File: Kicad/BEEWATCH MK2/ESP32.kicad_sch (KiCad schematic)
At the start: 38 parts, among them Q1 DMG6968U, SW1 TK-074-4, SW2 TK-074-4, U1 ESP32-S3, Y1 40MHz

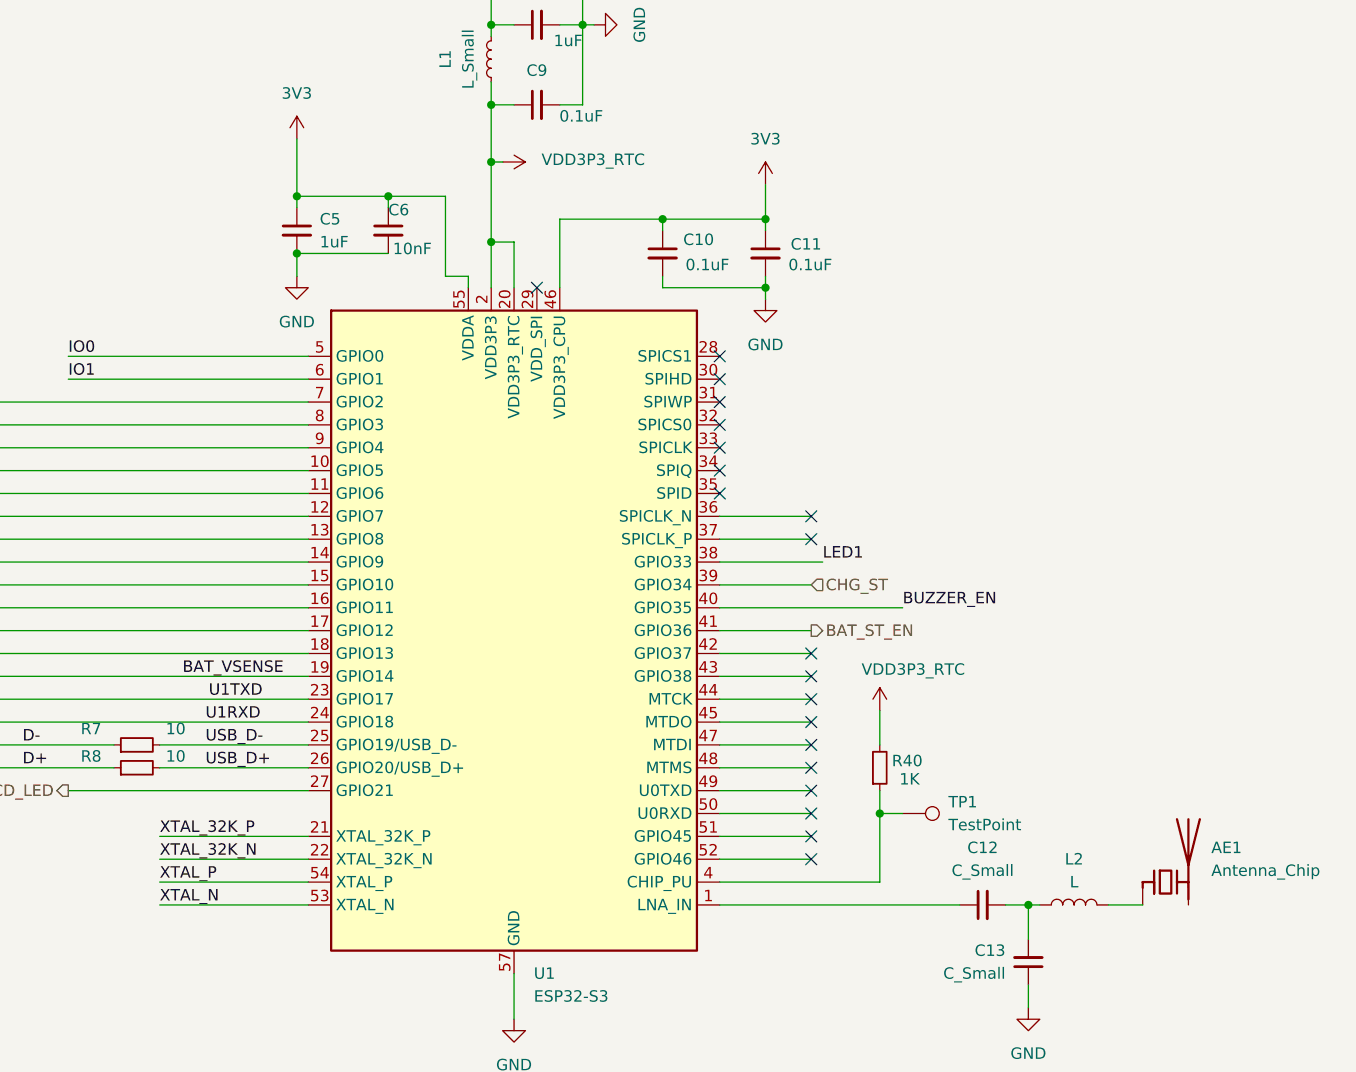
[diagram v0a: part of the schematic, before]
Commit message: Schematic changes
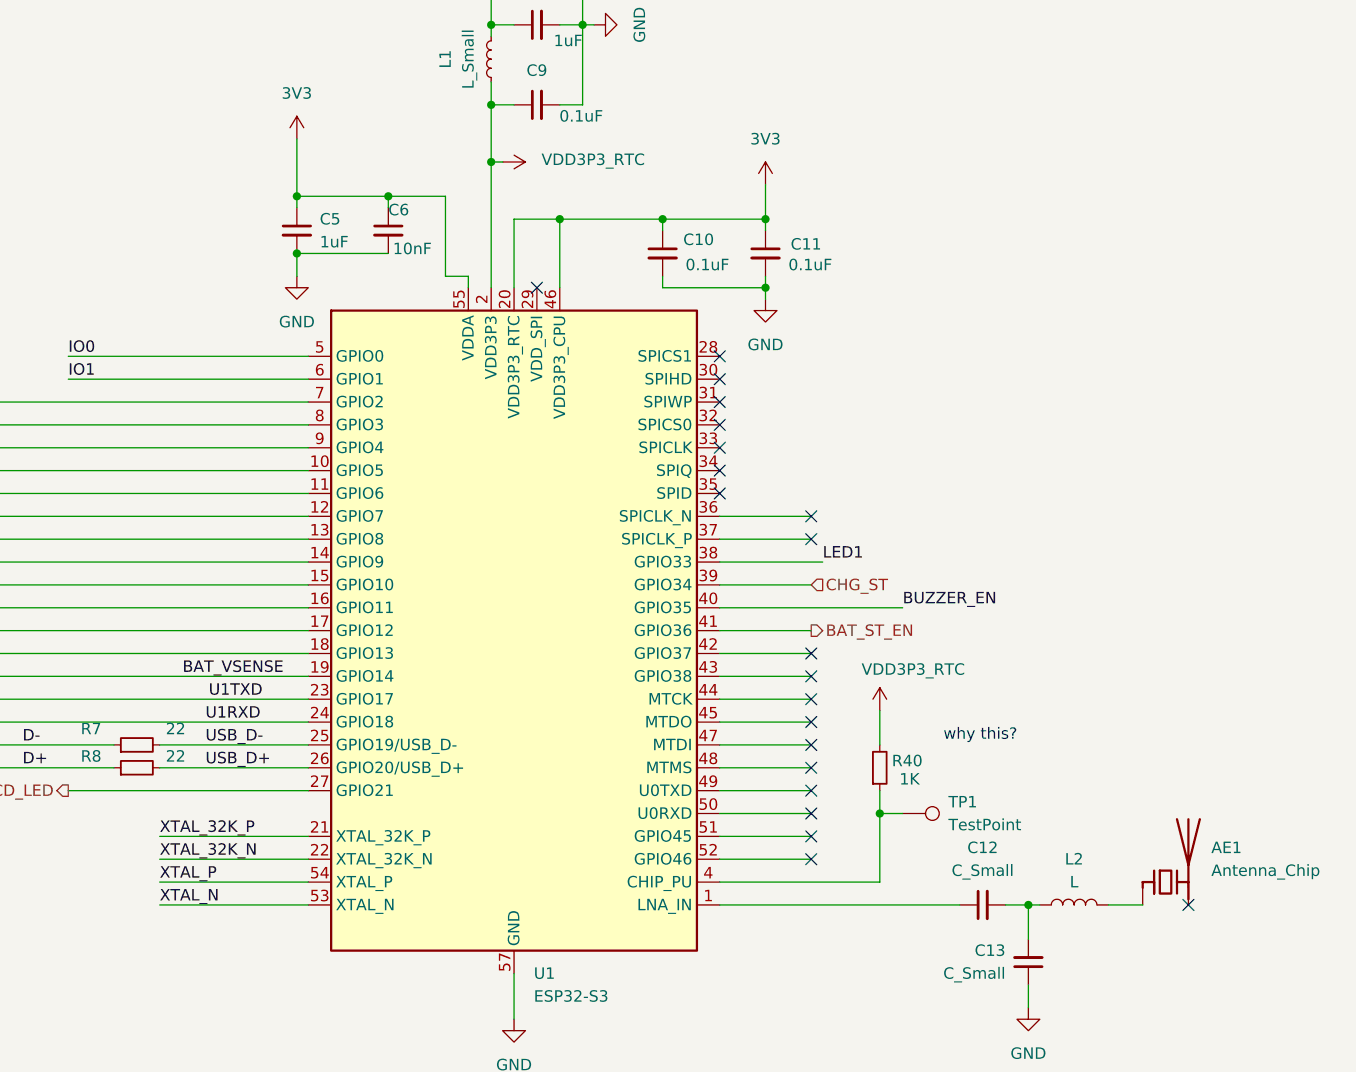
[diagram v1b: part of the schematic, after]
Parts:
- AE1: footprint (none) -> Project:ANT
- C10, C11, C12, C13, C5, C6, C7, C8, C9: footprint Capacitor_SMD:C_0603_1608Metric -> Capacitor_SMD:C_0402_1005Metric_Pad0.74x0.62mm_HandSolder
- R10, R23, R3, R4, R40, R5, R6, R9, R? (x2): footprint Resistor_SMD:R_0402_1005Metric -> Resistor_SMD:R_0402_1005Metric_Pad0.72x0.64mm_HandSolder
- R7, R8: value 10 -> 22; footprint Resistor_SMD:R_0402_1005Metric -> Resistor_SMD:R_0402_1005Metric_Pad0.72x0.64mm_HandSolder
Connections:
- net 3V3: now also U1.20 (VDD3P3_RTC)
- net VDD3P3_RTC: no longer U1.20 (VDD3P3_RTC)
- no-connect marks 23 -> 24
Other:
- note added: "why this?"
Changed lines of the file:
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@@
 	)
 	(junction
-		(at 270.51 85.09)
+		(at 278.13 82.55)
 		(diameter 0)
 		(color 0 0 0 0)
@@
 	)
 	(no_connect
+		(at 347.98 158.75)
+	)
+	(no_connect
 		(at 92.71 76.2)
 	)
@@
 	(wire
 		(pts
-			(xy 270.51 85.09) (xy 270.51 90.17)
-		)
-		(stroke
-			(width 0)
-			(type default)
-		)
-	)
-	(wire
-		(pts
 			(xy 100.33 246.38) (xy 100.33 247.65)
 		)
@@
 	(wire
 		(pts
+			(xy 273.05 82.55) (xy 273.05 90.17)
+		)
+		(stroke
+			(width 0)
+			(type default)
+		)
+	)
+	(wire
+		(pts
 			(xy 332.74 200.66) (xy 332.74 208.28)
 		)
@@
 	(wire
 		(pts
-			(xy 270.51 85.09) (xy 273.05 85.09)
-		)
-		(stroke
-			(width 0)
-			(type default)
-		)
-	)
-	(wire
-		(pts
 			(xy 248.92 80.01) (xy 248.92 81.28)
 		)
@@
 	(wire
 		(pts
-			(xy 273.05 90.17) (xy 273.05 85.09)
-		)
-		(stroke
-			(width 0)
-			(type default)
-		)
-	)
-	(wire
-		(pts
 			(xy 95.25 67.31) (xy 102.87 67.31)
 		)
@@
 	(wire
 		(pts
+			(xy 273.05 82.55) (xy 278.13 82.55)
+		)
+		(stroke
+			(width 0)
+			(type default)
+		)
+	)
+	(wire
+		(pts
 			(xy 100.33 246.38) (xy 106.68 246.38)
 		)
@@
 	(wire
 		(pts
-			(xy 270.51 76.2) (xy 270.51 85.09)
+			(xy 270.51 76.2) (xy 270.51 90.17)
 		)
 		(stroke
@@
 		)
 	)
+	(text "why this?\n"
+		(exclude_from_sim no)
+		(at 324.866 139.954 0)
+		(effects
+			(font
+				(size 1.27 1.27)
+			)
+		)
+	)
 	(text "ESP32-S3FH4R2"
 		(exclude_from_sim no)
@@
 			)
 		)
-		(property "Footprint" "Capacitor_SMD:C_0603_1608Metric"
+		(property "Footprint" "Capacitor_SMD:C_0402_1005Metric_Pad0.74x0.62mm_HandSolder"
 			(at 300.99 86.36 0)
 			(effects
@@
 			)
 		)
-		(property "Footprint" "Resistor_SMD:R_0402_1005Metric"
+		(property "Footprint" "Resistor_SMD:R_0402_1005Metric_Pad0.72x0.64mm_HandSolder"
 			(at 134.62 222.25 0)
 			(effects
@@
 			)
 		)
-		(property "Footprint" "Resistor_SMD:R_0402_1005Metric"
+		(property "Footprint" "Resistor_SMD:R_0402_1005Metric_Pad0.72x0.64mm_HandSolder"
 			(at 73.66 123.698 90)
 			(effects
@@
 			)
 		)
-		(property "Footprint" ""
+		(property "Footprint" "Project:ANT"
 			(at 342.9 151.765 0)
 			(effects
@@
 			)
 		)
-		(property "Footprint" "Resistor_SMD:R_0402_1005Metric"
+		(property "Footprint" "Resistor_SMD:R_0402_1005Metric_Pad0.72x0.64mm_HandSolder"
 			(at 100.33 53.34 0)
 			(effects
@@
 			)
 		)
-		(property "Footprint" "Capacitor_SMD:C_0603_1608Metric"
+		(property "Footprint" "Capacitor_SMD:C_0402_1005Metric_Pad0.74x0.62mm_HandSolder"
 			(at 330.2 165.1 0)
 			(effects
@@
 			)
 		)
-		(property "Value" "10"
+		(property "Value" "22"
 			(at 235.458 142.24 90)
 			(effects
@@
 			)
 		)
-		(property "Footprint" "Resistor_SMD:R_0402_1005Metric"
+		(property "Footprint" "Resistor_SMD:R_0402_1005Metric_Pad0.72x0.64mm_HandSolder"
 			(at 231.14 143.51 0)
 			(effects
@@
 			)
 		)
-		(property "Value" "10"
+		(property "Value" "22"
 			(at 235.458 139.192 90)
 			(effects
@@
 			)
 		)
-		(property "Footprint" "Resistor_SMD:R_0402_1005Metric"
+		(property "Footprint" "Resistor_SMD:R_0402_1005Metric_Pad0.72x0.64mm_HandSolder"
 			(at 231.14 140.97 0)
 			(effects
@@
 			)
 		)
-		(property "Footprint" "Capacitor_SMD:C_0603_1608Metric"
+		(property "Footprint" "Capacitor_SMD:C_0402_1005Metric_Pad0.74x0.62mm_HandSolder"
 			(at 259.08 83.82 0)
 			(effects
@@
 			)
 		)
-		(property "Footprint" "Resistor_SMD:R_0402_1005Metric"
+		(property "Footprint" "Resistor_SMD:R_0402_1005Metric_Pad0.72x0.64mm_HandSolder"
 			(at 100.33 55.88 0)
 			(effects
@@
 			)
 		)
-		(property "Footprint" "Capacitor_SMD:C_0603_1608Metric"
+		(property "Footprint" "Capacitor_SMD:C_0402_1005Metric_Pad0.74x0.62mm_HandSolder"
 			(at 275.59 60.96 0)
 			(effects
@@
 			)
 		)
-		(property "Footprint" "Resistor_SMD:R_0402_1005Metric"
+		(property "Footprint" "Resistor_SMD:R_0402_1005Metric_Pad0.72x0.64mm_HandSolder"
 			(at 218.44 215.9 0)
 			(effects
@@
 			)
 		)
-		(property "Footprint" "Resistor_SMD:R_0402_1005Metric"
+		(property "Footprint" "Resistor_SMD:R_0402_1005Metric_Pad0.72x0.64mm_HandSolder"
 			(at 318.77 224.79 0)
 			(effects
@@
 			)
 		)
-		(property "Footprint" "Capacitor_SMD:C_0603_1608Metric"
+		(property "Footprint" "Capacitor_SMD:C_0402_1005Metric_Pad0.74x0.62mm_HandSolder"
 			(at 325.12 158.75 0)
 			(effects
@@
 			)
 		)
-		(property "Footprint" "Resistor_SMD:R_0402_1005Metric"
+		(property "Footprint" "Resistor_SMD:R_0402_1005Metric_Pad0.72x0.64mm_HandSolder"
 			(at 100.33 222.25 0)
 			(effects
@@
 			)
 		)
-		(property "Footprint" "Capacitor_SMD:C_0603_1608Metric"
+		(property "Footprint" "Capacitor_SMD:C_0402_1005Metric_Pad0.74x0.62mm_HandSolder"
 			(at 289.56 86.36 0)
 			(effects
@@
 			)
 		)
-		(property "Footprint" "Resistor_SMD:R_0402_1005Metric"
+		(property "Footprint" "Resistor_SMD:R_0402_1005Metric_Pad0.72x0.64mm_HandSolder"
 			(at 119.38 131.318 90)
 			(effects
@@
 			)
 		)
-		(property "Footprint" "Capacitor_SMD:C_0603_1608Metric"
+		(property "Footprint" "Capacitor_SMD:C_0402_1005Metric_Pad0.74x0.62mm_HandSolder"
 			(at 275.59 50.8 0)
 			(effects
@@
 			)
 		)
-		(property "Footprint" "Resistor_SMD:R_0402_1005Metric"
+		(property "Footprint" "Resistor_SMD:R_0402_1005Metric_Pad0.72x0.64mm_HandSolder"
 			(at 323.85 231.14 0)
 			(effects
@@
 			)
 		)
-		(property "Footprint" "Resistor_SMD:R_0402_1005Metric"
+		(property "Footprint" "Resistor_SMD:R_0402_1005Metric_Pad0.72x0.64mm_HandSolder"
 			(at 313.69 143.51 0)
 			(effects
@@
 			)
 		)
-		(property "Footprint" "Capacitor_SMD:C_0603_1608Metric"
+		(property "Footprint" "Capacitor_SMD:C_0402_1005Metric_Pad0.74x0.62mm_HandSolder"
 			(at 248.92 83.82 0)
 			(effects
@@
 			)
 		)
-		(property "Footprint" "Capacitor_SMD:C_0603_1608Metric"
+		(property "Footprint" "Capacitor_SMD:C_0402_1005Metric_Pad0.74x0.62mm_HandSolder"
 			(at 275.59 69.85 0)
 			(effects

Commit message: GNSS level shifter floating voltage needs to be fix
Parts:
- Y1: footprint Crystal:Crystal_SMD_1210-4Pin_1.2x1.0mm -> Crystal:Crystal_SMD_2016-4Pin_2.0x1.6mm
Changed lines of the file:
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@@
 			)
 		)
-		(property "Footprint" "Crystal:Crystal_SMD_1210-4Pin_1.2x1.0mm"
+		(property "Footprint" "Crystal:Crystal_SMD_2016-4Pin_2.0x1.6mm"
 			(at 73.66 139.7 0)
 			(effects

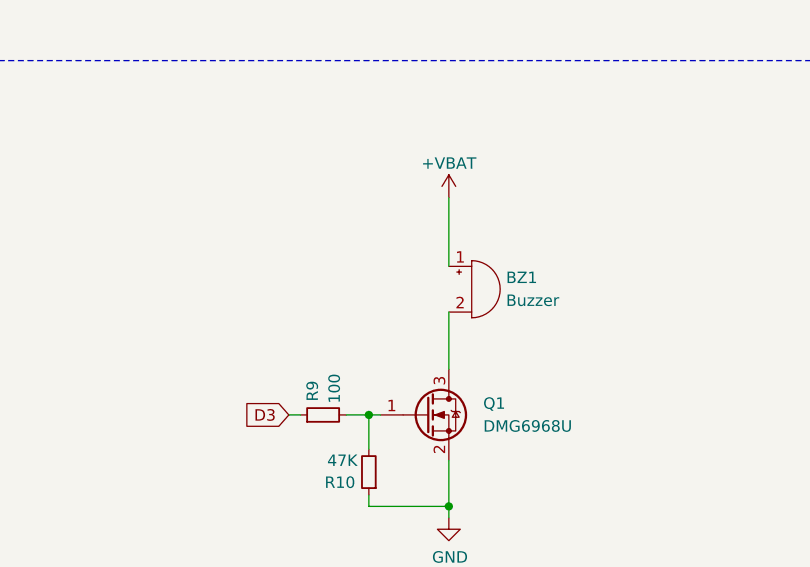
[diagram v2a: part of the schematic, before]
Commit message: Added Buzzer flyback diode
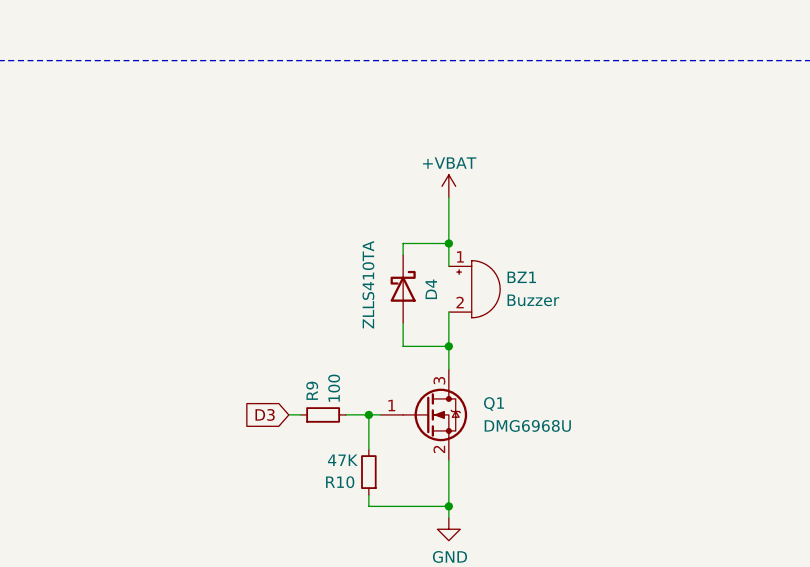
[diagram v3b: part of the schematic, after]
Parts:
- added D4: ZLLS410TA, Diode_SMD:D_SOD-323F, symbol Device:D_Schottky
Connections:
- net +VBAT: now also D4.1 (K)
- net at BZ1.2 (-), Q1.3 (D): now also D4.2 (A)
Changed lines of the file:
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@@
 	)
 	(junction
+		(at 332.74 205.74)
+		(diameter 0)
+		(color 0 0 0 0)
+	)
+	(junction
+		(at 332.74 217.17)
+		(diameter 0)
+		(color 0 0 0 0)
+	)
+	(junction
 		(at 119.38 158.75)
 		(diameter 0)
@@
 	(wire
 		(pts
+			(xy 327.66 207.01) (xy 327.66 205.74)
+		)
+		(stroke
+			(width 0)
+			(type default)
+		)
+	)
+	(wire
+		(pts
 			(xy 295.91 118.11) (xy 306.07 118.11)
 		)
@@
 	(wire
 		(pts
+			(xy 332.74 205.74) (xy 332.74 208.28)
+		)
+		(stroke
+			(width 0)
+			(type default)
+		)
+	)
+	(wire
+		(pts
 			(xy 116.84 229.87) (xy 100.33 229.87)
 		)
@@
 	(wire
 		(pts
-			(xy 332.74 200.66) (xy 332.74 208.28)
+			(xy 332.74 200.66) (xy 332.74 205.74)
 		)
 		(stroke
@@
 	(wire
 		(pts
+			(xy 327.66 205.74) (xy 332.74 205.74)
+		)
+		(stroke
+			(width 0)
+			(type default)
+		)
+	)
+	(wire
+		(pts
 			(xy 212.09 125.73) (xy 250.19 125.73)
 		)
@@
 	(wire
 		(pts
+			(xy 332.74 217.17) (xy 332.74 219.71)
+		)
+		(stroke
+			(width 0)
+			(type default)
+		)
+	)
+	(wire
+		(pts
 			(xy 248.92 80.01) (xy 248.92 81.28)
 		)
@@
 	(wire
 		(pts
-			(xy 332.74 213.36) (xy 332.74 219.71)
+			(xy 332.74 213.36) (xy 332.74 217.17)
 		)
 		(stroke
@@
 	(wire
 		(pts
+			(xy 327.66 217.17) (xy 332.74 217.17)
+		)
+		(stroke
+			(width 0)
+			(type default)
+		)
+	)
+	(wire
+		(pts
 			(xy 67.31 139.7) (xy 67.31 148.59)
 		)
@@
 	(wire
 		(pts
+			(xy 327.66 214.63) (xy 327.66 217.17)
+		)
+		(stroke
+			(width 0)
+			(type default)
+		)
+	)
+	(wire
+		(pts
 			(xy 67.31 157.48) (xy 73.66 157.48)
 		)
@@
 					(unit 1)
 				)
+			)
+		)
+	)
+	(symbol
+		(lib_id "Device:D_Schottky")
+		(at 327.66 210.82 270)
+		(unit 1)
+		(exclude_from_sim no)
+		(in_bom yes)
+		(on_board yes)
+		(dnp no)
+		(property "Reference" "D4"
+			(at 330.835 212.09 0)
+			(effects
+				(font
+					(size 1.27 1.27)
+				)
+				(justify right)
+			)
+		)
+		(property "Value" "ZLLS410TA"
+			(at 323.85 215.265 0)
+			(effects
+				(font
+					(size 1.27 1.27)
+				)
+				(justify right)
+			)
+		)
+		(property "Footprint" "Diode_SMD:D_SOD-323F"
+			(at 327.66 210.82 0)
+			(effects
+				(font
+					(size 1.27 1.27)
+				)
+				(hide yes)
+			)
+		)
+		(property "Datasheet" "~"
+			(at 327.66 210.82 0)
+			(effects
+				(font
+					(size 1.27 1.27)
+				)
+				(hide yes)
+			)
+		)
+		(property "Description" "Schottky diode"
+			(at 327.66 210.82 0)
+			(effects
+				(font
+					(size 1.27 1.27)
+				)
+				(hide yes)
+			)
+		)
+		(pin "1"
+		)
+		(pin "2"
+		)
+		(instances
+			(project "BEEWATCH MK3"
+				(path "/e9c5fb53-480b-4989-8495-a3341ee99514/56d77f8e-c069-456f-a514-fdde13f048cd"
+					(reference "D4")
+					(unit 1)
+				)

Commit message: Updated with sub module lib
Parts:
- AE1: footprint Project:ANT -> ANTENNA:RYS8830_ANT
- BZ1: footprint Project:CL9032A-CLDZ-SMD Passive Buzzer -> SM_BUZZER:CL9032A-CLDZ-SMD Passive Buzzer
- D1: footprint Project:XL-0807RGBC-WS2812B -> SM_LED:XL-0807RGBC-WS2812B
- SW1, SW2: footprint Project:Tact Switch-TK-074-4 Pin SMD -> SM_SWITCH:Tact Switch-TK-074-4 Pin SMD
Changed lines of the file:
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@@
 			)
 		)
-		(property "Footprint" "Project:Tact Switch-TK-074-4 Pin SMD"
+		(property "Footprint" "SM_SWITCH:Tact Switch-TK-074-4 Pin SMD"
 			(at 134.62 233.68 0)
 			(effects
@@
 			)
 		)
-		(property "Footprint" "Project:XL-0807RGBC-WS2812B"
+		(property "Footprint" "SM_LED:XL-0807RGBC-WS2812B"
 			(at 201.93 229.87 0)
 			(effects
@@
 			)
 		)
-		(property "Footprint" "Project:ANT"
+		(property "Footprint" "ANTENNA:RYS8830_ANT"
 			(at 342.9 151.765 0)
 			(effects
@@
 			)
 		)
-		(property "Footprint" "Project:Tact Switch-TK-074-4 Pin SMD"
+		(property "Footprint" "SM_SWITCH:Tact Switch-TK-074-4 Pin SMD"
 			(at 100.33 232.41 0)
 			(effects
@@
 			)
 		)
-		(property "Footprint" "Project:CL9032A-CLDZ-SMD Passive Buzzer"
+		(property "Footprint" "SM_BUZZER:CL9032A-CLDZ-SMD Passive Buzzer"
 			(at 334.645 208.28 90)
 			(effects

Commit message: Lib Integration almost done
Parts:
- AE1: footprint ANTENNA:RYS8830_ANT -> ANTENNA:ESP32_ZERO_ANT
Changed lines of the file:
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@@
 			)
 		)
-		(property "Footprint" "ANTENNA:RYS8830_ANT"
+		(property "Footprint" "ANTENNA:ESP32_ZERO_ANT"
 			(at 342.9 151.765 0)
 			(effects

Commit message: minor change in ESP32
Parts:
- added R51, R52: 0, Resistor_SMD:R_0402_1005Metric_Pad0.72x0.64mm_HandSolder, symbol Device:R_Small
- U1: value ESP32-S3 -> ESP32-S3FH4R2
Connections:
- net GND: now also R51.2, R52.1
- net at U1.51 (GPIO45): now also R51.1
- net at U1.52 (GPIO46): now also R52.2
- no-connect marks 24 -> 22
